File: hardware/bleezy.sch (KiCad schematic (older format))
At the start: 37 parts, among them IC1 NRF51822, P1 Analog Header, P2 Digital Con 2, P3 Raspberry_Pi_+_Conn, P5 Power Con, P6 TST, U1 LD3985M33R, Y1 32Khz, Y2 16Mhz

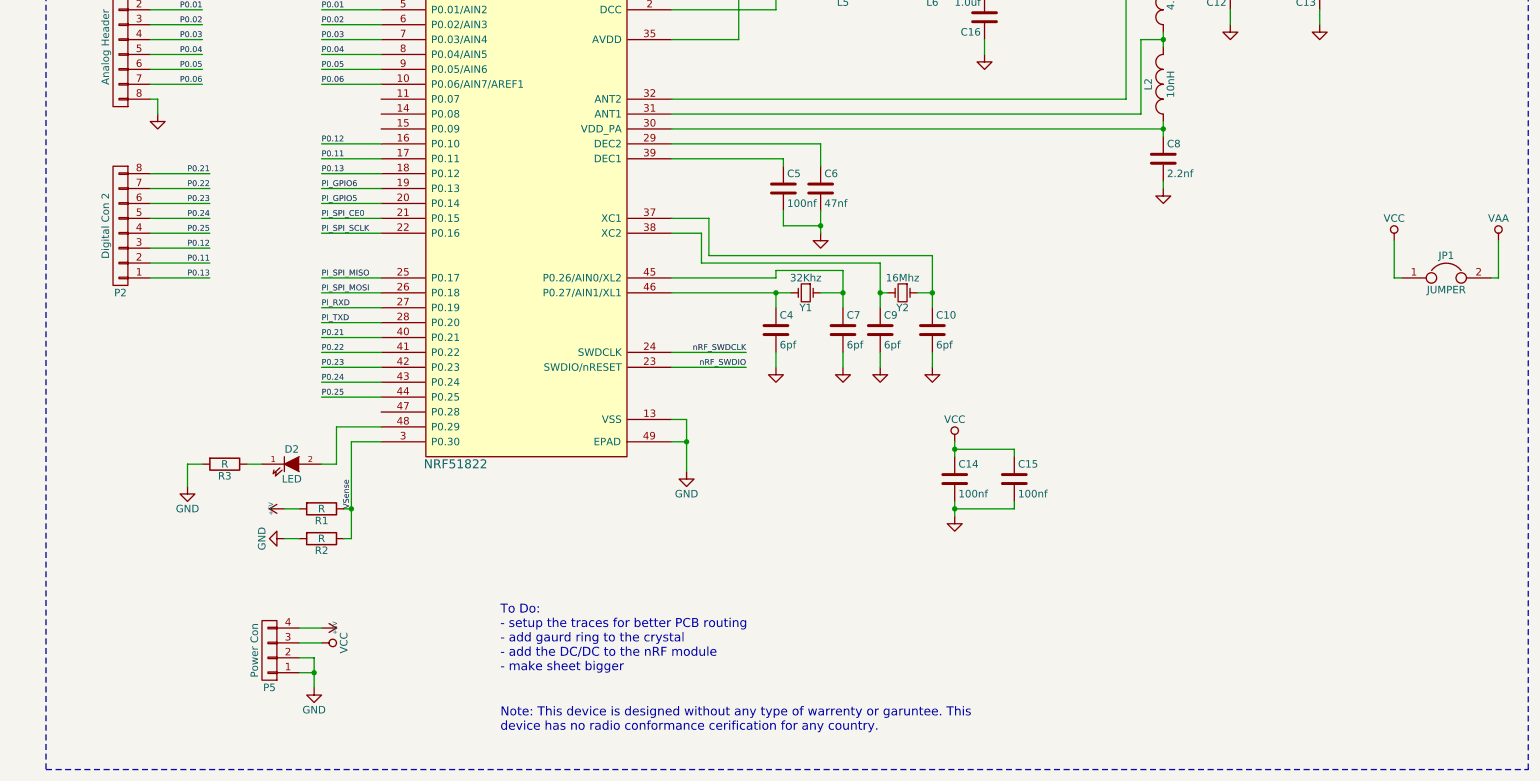
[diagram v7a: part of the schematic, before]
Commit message: added part numbers to component feilds
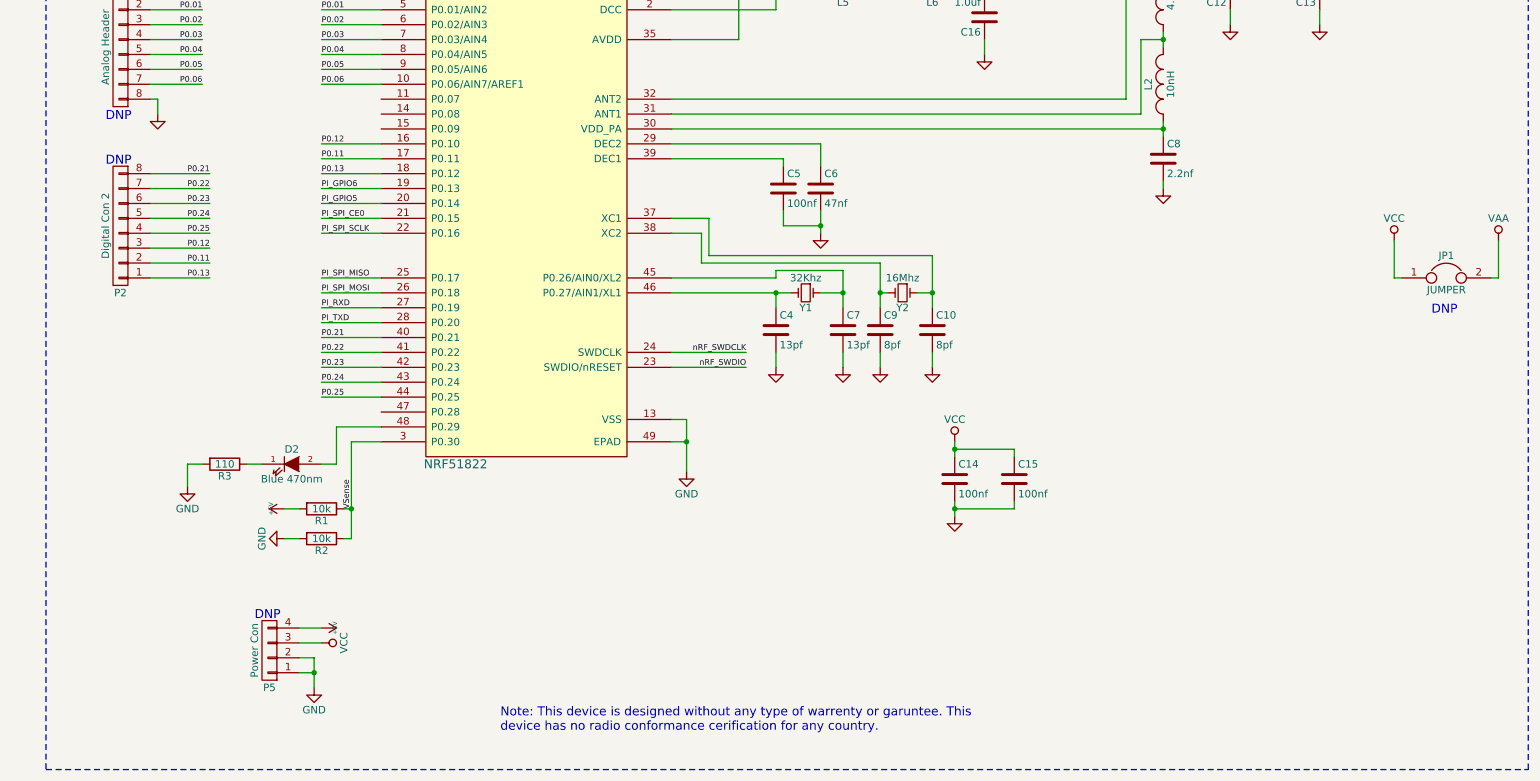
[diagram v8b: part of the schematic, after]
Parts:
- BT1: Mouser Part No. (none) -> 534-3003
- C1: Mouser Part No. (none) -> 581-04026D225KAT2A
- C10, C9: value 6pf -> 8pf; Mouser Part No. (none) -> 81-GRM1555C1H8R0DA1D
- C11: Mouser Part No. (none) -> 81-GRM1555C1H2R2BA1D
- C12: Mouser Part No. (none) -> GRM1555C1H1R0CA01D
- C13: Mouser Part No. (none) -> GRM1555C1H1R5BA01D
- C14, C15, C5: Mouser Part No. (none) -> 81-GRM155R71C104KA88
- C16: Mouser Part No. (none) -> 81-GRM155R61A105KE15
- C2: Mouser Part No. (none) -> 581-06036D105K
- C3: Mouser Part No. (none) -> 581-TAJB106K006R
- C4, C7: value 6pf -> 13pf; Mouser Part No. (none) -> 81-GRM1555C1H130JA1D
- C6: Mouser Part No. (none) -> 81-GRM15B11A473KA01D
- C8: Mouser Part No. (none) -> GRM155R71H222KA01D
- D2: value LED -> Blue 470nm; Mouser Part No. (none) -> 859-LTST-C191TBKT-5A
- IC1: Mouser Part No. (none) -> 949-NRF51822-QFAA-R7
- L1: Mouser Part No. (none) -> 81-LQW15AN4N7C00D
- L2: Mouser Part No. (none) -> 994-0402HP-10NXJLU
- L5: Mouser Part No. (none) -> 963-LK1608100K-T
- L6: Mouser Part No. (none) -> 81-LQW15AN15NJ00D
- P3: Mouser Part No. 517-30340-6002 -> 517-929975-01-20
- R1, R2: value R -> 10k; Mouser Part No. (none) -> 754-RR0510P-103D
- R3: value R -> 110; Mouser Part No. (none) -> 754-RR0510P-111D
- U1: Mouser Part No. (none) -> 511-LD3985M33R
- Y1: Mouser Part No. (none) -> 815-AB38T-32.768KHZ
- Y2: Mouser Part No. (none) -> 581-CX2520DB16DGEJCC
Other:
- note added: "DNP"
- note removed: "To Do:\n- setup the traces for better PCB routing\n- add gaurd ring to the crystal\n- add the DC/DC to the nRF module\n- make sheet bigger"
